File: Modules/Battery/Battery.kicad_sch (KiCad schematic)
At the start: 0 parts

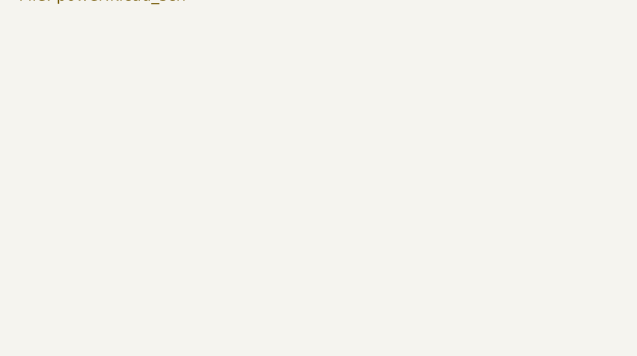
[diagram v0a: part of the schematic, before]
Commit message: update to I2C and MIDI Interface
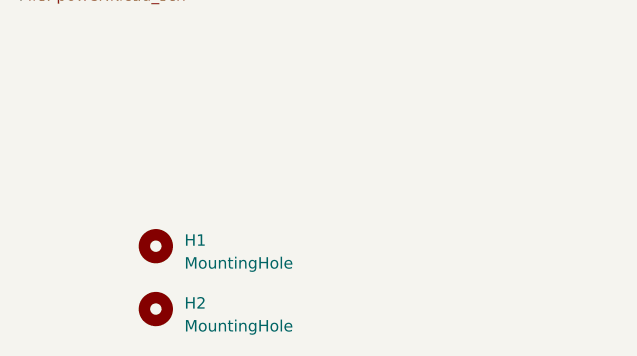
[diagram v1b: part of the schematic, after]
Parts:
- added H1, H2: MountingHole, symbol Mechanical:MountingHole
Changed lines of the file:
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@@
     (company "FG Labs")
+  )
+  (symbol (lib_id "Mechanical:MountingHole") (at 40.005 96.52 0) (unit 1)
+    (in_bom yes) (on_board yes) (dnp no) (fields_autoplaced)
+    (property "Reference" "H1" (at 43.18 95.885 0)
+      (effects (font (size 1.27 1.27)) (justify left))
+    )
+    (property "Value" "MountingHole" (at 43.18 98.425 0)
+      (effects (font (size 1.27 1.27)) (justify left))
+    )
+    (property "Footprint" "" (at 40.005 96.52 0)
+      (effects (font (size 1.27 1.27)) hide)
+    )
+    (property "Datasheet" "~" (at 40.005 96.52 0)
+      (effects (font (size 1.27 1.27)) hide)
+    )
+    (instances
+      (project "Battery"
+        (path "/5e90b4be-f726-48f1-ba15-bc9158342c0e"
+          (reference "H1") (unit 1)
+        )
+      )
+    )
+  )
+  (symbol (lib_id "Mechanical:MountingHole") (at 40.005 103.505 0) (unit 1)
+    (in_bom yes) (on_board yes) (dnp no) (fields_autoplaced)
+    (property "Reference" "H2" (at 43.18 102.87 0)
+      (effects (font (size 1.27 1.27)) (justify left))
+    )
+    (property "Value" "MountingHole" (at 43.18 105.41 0)
+      (effects (font (size 1.27 1.27)) (justify left))
+    )
+    (property "Footprint" "" (at 40.005 103.505 0)
+      (effects (font (size 1.27 1.27)) hide)
+    )
+    (property "Datasheet" "~" (at 40.005 103.505 0)
+      (effects (font (size 1.27 1.27)) hide)
+    )
+    (instances
+      (project "Battery"
+        (path "/5e90b4be-f726-48f1-ba15-bc9158342c0e"
+          (reference "H2") (unit 1)
+        )
+      )
+    )
   )
   (sheet (at 106.68 23.495) (size 80.645 44.45) (fields_autoplaced)

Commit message: first rev of Battery module
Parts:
- H1, H2: footprint (none) -> MountingHole:MountingHole_3.2mm_M3_DIN965; now left out of the parts list
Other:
- note added: "Place Mounting holes werever Use Cable to attach to main PCB"
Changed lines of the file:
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@@
     (company "FG Labs")
   )
+  (text "Place Mounting holes werever\nUse Cable to attach to main PCB"
+    (at 64.77 102.87 0)
+    (effects (font (size 1.27 1.27)) (justify left bottom))
+  )
   (symbol (lib_id "Mechanical:MountingHole") (at 40.005 96.52 0) (unit 1)
-    (in_bom yes) (on_board yes) (dnp no) (fields_autoplaced)
+    (in_bom no) (on_board yes) (dnp no) (fields_autoplaced)
     (property "Reference" "H1" (at 43.18 95.885 0)
       (effects (font (size 1.27 1.27)) (justify left))
@@
       (effects (font (size 1.27 1.27)) (justify left))
     )
-    (property "Footprint" "" (at 40.005 96.52 0)
+    (property "Footprint" "MountingHole:MountingHole_3.2mm_M3_DIN965" (at 40.005 96.52 0)
       (effects (font (size 1.27 1.27)) hide)
     )
@@
   )
   (symbol (lib_id "Mechanical:MountingHole") (at 40.005 103.505 0) (unit 1)
-    (in_bom yes) (on_board yes) (dnp no) (fields_autoplaced)
+    (in_bom no) (on_board yes) (dnp no) (fields_autoplaced)
     (property "Reference" "H2" (at 43.18 102.87 0)
       (effects (font (size 1.27 1.27)) (justify left))
@@
       (effects (font (size 1.27 1.27)) (justify left))
     )
-    (property "Footprint" "" (at 40.005 103.505 0)
+    (property "Footprint" "MountingHole:MountingHole_3.2mm_M3_DIN965" (at 40.005 103.505 0)
       (effects (font (size 1.27 1.27)) hide)
     )
